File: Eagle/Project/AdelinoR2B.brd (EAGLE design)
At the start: 47 x 53.3 mm, 70 parts, among them J1 DC-044-A, J2 YELLOW-8P-2.54, J3 YELLOW-6P-2.54, J4 YELLOW-8P-2.54, J5 YELLOW-8P-2.54, J6 4P-2.0, J7 YELLOW-2X3P-2.54, J8 4P-2.0, Q1 NCE3407A, Q2 CJ2305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

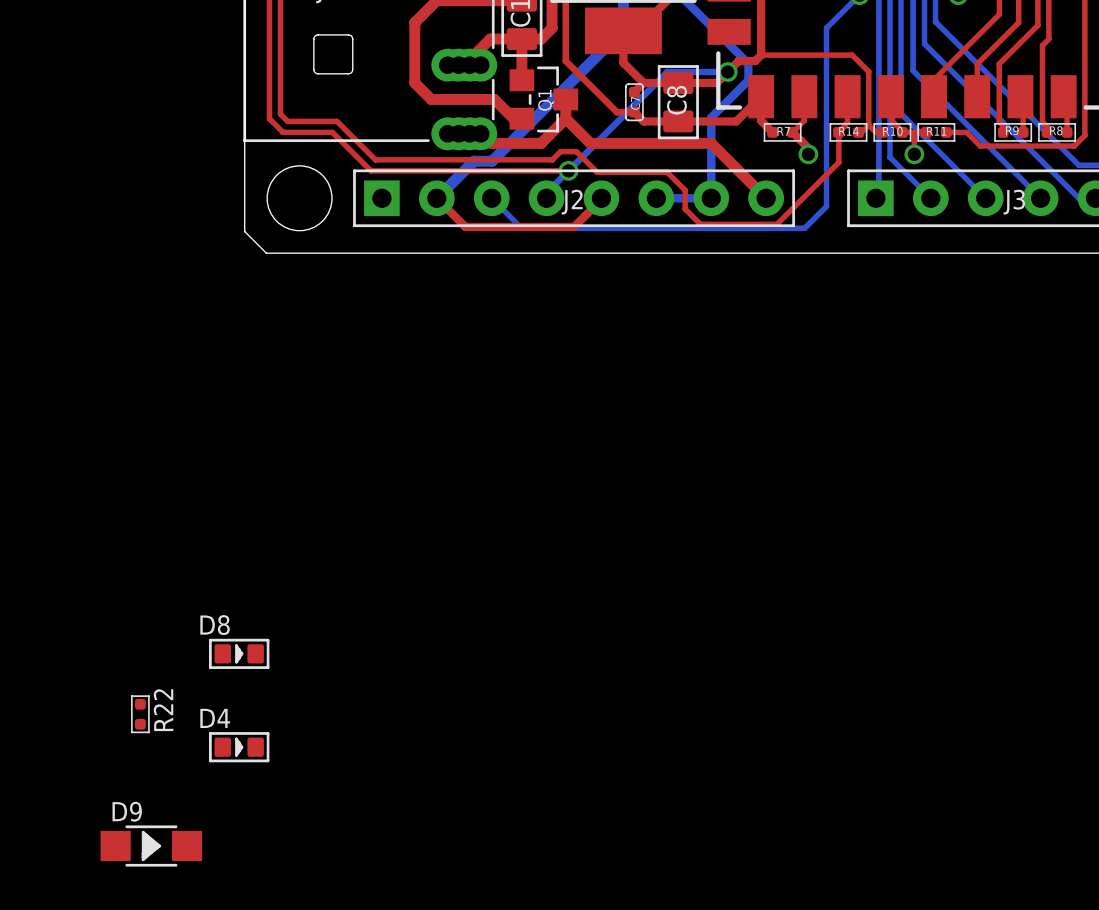
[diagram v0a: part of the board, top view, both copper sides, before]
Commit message: Update GPIO0 wires.
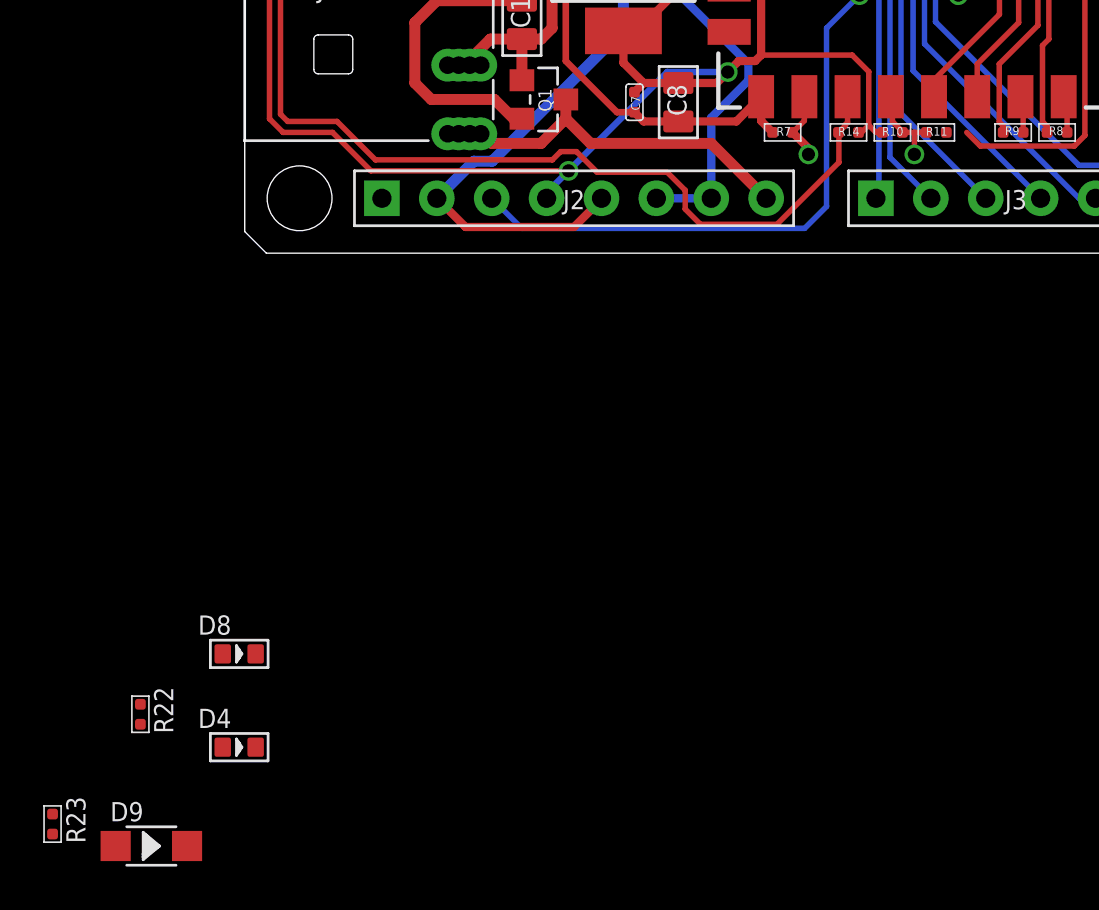
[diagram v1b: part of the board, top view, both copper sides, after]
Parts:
- added R23: 1K, Seeed-Resistor:R0402
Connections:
- new net ESP_PROG: R11.2, R23.2
- net MOSI: no longer R11.2
- net PB0_RX_LED: now also R23.1
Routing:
- net MOSI: track 48.5 -> 47.5 mm
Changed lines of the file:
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@@
 <attribute name="VALUE" x="-6.223" y="-29.464" size="0.889" layer="27" font="vector" ratio="11"/>
+</element>
+<element name="R23" library="Seeed-Resistor" package="R0402" value="1K" x="-8.89" y="-26.416" smashed="yes">
+<attribute name="MPN" value="RC0402JR-071KL" x="-8.89" y="-26.416" size="1.778" layer="27" display="off"/>
+<attribute name="NAME" x="-8.255" y="-25.146" size="0.889" layer="25" ratio="11" rot="R270"/>
+<attribute name="VALUE" x="-10.414" y="-25.146" size="0.889" layer="27" font="vector" ratio="11" rot="R270"/>
 </element>
 </elements>
@@
 <contactref element="U4" pad="10"/>
 <contactref element="J7" pad="5"/>
-<contactref element="R11" pad="2"/>
 <wire x1="44.45" y1="27.94" x2="43.7515" y2="27.2415" width="0.254" layer="1"/>
 <wire x1="43.7515" y1="27.2415" x2="43.033075" y2="27.2415" width="0.254" layer="1"/>
@@
 <wire x1="38.38909375" y1="4.957" x2="34.0411875" y2="4.957" width="0.254" layer="1"/>
 <wire x1="34.0411875" y1="4.957" x2="33.4101875" y2="5.588" width="0.254" layer="1"/>
-<wire x1="33.4101875" y1="5.588" x2="32.4665" y2="5.588" width="0.254" layer="1"/>
 <wire x1="41.41025" y1="26.6065" x2="40.20375" y2="25.4" width="0.254" layer="1"/>
 <wire x1="40.20375" y1="25.4" x2="39.37" y2="25.4" width="0.254" layer="1"/>
@@
 <contactref element="U4" pad="8"/>
 <contactref element="R18" pad="1"/>
+<contactref element="R23" pad="1"/>
 <wire x1="1.9505" y1="27.178" x2="38.312" y2="36.398" width="0" layer="19" extent="1-1"/>
+<wire x1="-8.89" y1="-25.9535" x2="1.9505" y2="27.178" width="0" layer="19" extent="1-1"/>
 </signal>
 <signal name="PD5_TX_LED">
@@
 <wire x1="-4.826" y1="-20.8735" x2="28.512" y2="40.598" width="0" layer="19" extent="1-1"/>
 </signal>
+<signal name="ESP_PROG">
+<contactref element="R23" pad="2"/>
+<contactref element="R11" pad="2"/>
+<wire x1="-8.89" y1="-26.8785" x2="32.4665" y2="5.588" width="0" layer="19" extent="1-1"/>
+</signal>
 </signals>

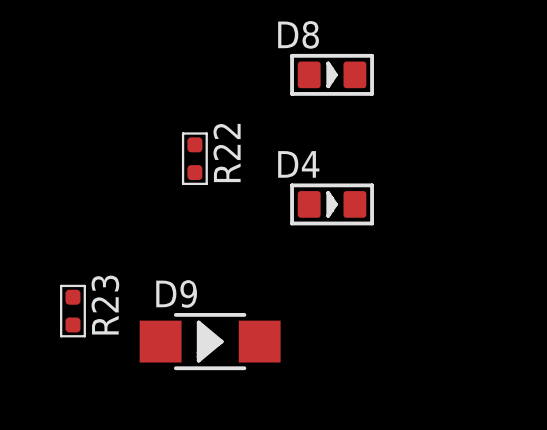
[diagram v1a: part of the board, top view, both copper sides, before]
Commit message: Remove redundant resistor from GPIO0 wiring.
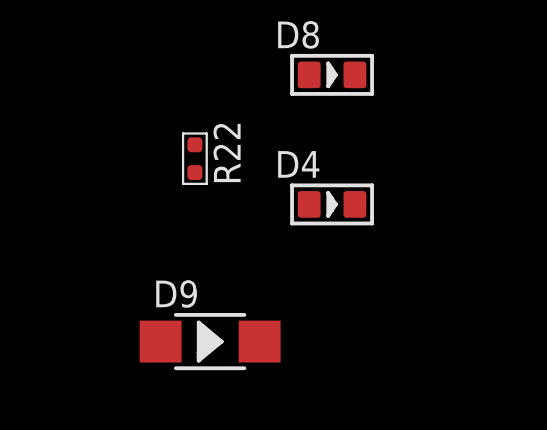
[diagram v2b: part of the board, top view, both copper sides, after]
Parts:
- removed R23: 1K, Seeed-Resistor:R0402
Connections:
- removed net N$6: D5.+, R18.2
- net ESP_PROG: now also D5.+, R18.2; no longer R23.2
- net PB0_RX_LED: no longer R23.1
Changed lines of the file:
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@@
 <attribute name="VALUE" x="-6.223" y="-29.464" size="0.889" layer="27" font="vector" ratio="11"/>
-</element>
-<element name="R23" library="Seeed-Resistor" package="R0402" value="1K" x="-8.89" y="-26.416" smashed="yes">
-<attribute name="MPN" value="RC0402JR-071KL" x="-8.89" y="-26.416" size="1.778" layer="27" display="off"/>
-<attribute name="NAME" x="-8.255" y="-25.146" size="0.889" layer="25" ratio="11" rot="R270"/>
-<attribute name="VALUE" x="-10.414" y="-25.146" size="0.889" layer="27" font="vector" ratio="11" rot="R270"/>
 </element>
 </elements>
@@
 <wire x1="1.9505" y1="29.718" x2="1.524" y2="30.988" width="0" layer="19" extent="1-1"/>
 </signal>
-<signal name="N$6">
-<contactref element="R18" pad="2"/>
-<contactref element="D5" pad="+"/>
-<wire x1="1.524" y1="28.448" x2="2.8755" y2="27.178" width="0" layer="19" extent="1-1"/>
-</signal>
 <signal name="N$8">
 <contactref element="R22" pad="2"/>
@@
 <contactref element="U4" pad="8"/>
 <contactref element="R18" pad="1"/>
-<contactref element="R23" pad="1"/>
 <wire x1="1.9505" y1="27.178" x2="38.312" y2="36.398" width="0" layer="19" extent="1-1"/>
-<wire x1="-8.89" y1="-25.9535" x2="1.9505" y2="27.178" width="0" layer="19" extent="1-1"/>
 </signal>
 <signal name="PD5_TX_LED">
@@
 </signal>
 <signal name="ESP_PROG">
-<contactref element="R23" pad="2"/>
 <contactref element="R11" pad="2"/>
-<wire x1="-8.89" y1="-26.8785" x2="32.4665" y2="5.588" width="0" layer="19" extent="1-1"/>
+<contactref element="R18" pad="2"/>
+<contactref element="D5" pad="+"/>
+<wire x1="2.8755" y1="27.178" x2="32.4665" y2="5.588" width="0" layer="19" extent="1-1"/>
+<wire x1="1.524" y1="28.448" x2="2.8755" y2="27.178" width="0" layer="19" extent="1-1"/>
 </signal>
 </signals>

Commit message: Adding native SPI support.
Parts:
- removed Q3, Q4: MMBT3904LT1G, Seeed-Transistor:SOT-23
- removed R12, R13: 1K, Seeed-Resistor:R0402
- added R23, R24, R25, R26: 1K, Seeed-Resistor:R0402
- R5, R6: value 10K 1/16W -> 10K
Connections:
- removed net HSPI_CLK: U3.5
- removed net HSPI_MISO: U3.6
- removed net HSPI_MOSI: U3.7
- removed net MISO: J7.1, U4.11
- removed net MOSI: J7.5, U4.10
- removed net N$16: Q3.1, R12.2
- removed net N$21: Q4.1, R13.2
- removed net N$4: R7.2, U3.16
- removed net PB0_RX_LED: R18.1, U4.8
- removed net SCK: J7.2, U4.9
- removed net STANDBY1: Q3.3
- removed net STANDBY2: Q4.3
- new net N$15: D5.+, R18.2
- new net N$19: R24.2, U3.7
- new net N$20: R25.2, U3.5
- new net N$22: R26.2, R7.2, U3.16
- new net N$6: R23.2, U3.6
- new net PB0_SS_RX: R18.1, R26.1, U4.8
- new net PB1_SCLK: J7.2, R25.1, U4.9
- new net PB2_MOSI: J7.5, R24.1, U4.10
- new net PB3_MISO: J7.1, R23.1, U4.11
- net ESP_PROG: no longer D5.+, R18.2
- net GND: no longer Q3.2, Q4.2
- net PIN_D13: no longer R13.1
- net PIN_D5: no longer R12.1
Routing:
- net PB2_MOSI: track 0.00 -> 47.5 mm, vias 0 -> 1
- net MOSI: track 47.5 -> 0.00 mm, vias 1 -> 0
- net SCK: track 18.0 -> 0.00 mm, vias 1 -> 0
- net PB1_SCLK: track 0.00 -> 18.0 mm, vias 0 -> 1
- net PB3_MISO: track 0.00 -> 15.1 mm, vias 0 -> 1
- net MISO: track 15.1 -> 0.00 mm, vias 1 -> 0
- net GND: track 296.2 -> 287.0 mm
- net N$20: track 0.00 -> 8.44 mm, vias 0 -> 1
- net HSPI_CLK: track 8.44 -> 0.00 mm, vias 1 -> 0
- net N$6: track 0.00 -> 5.84 mm, vias 0 -> 1
- net HSPI_MISO: track 5.84 -> 0.00 mm, vias 1 -> 0
- net N$19: track 0.00 -> 3.23 mm, vias 0 -> 1
- net HSPI_MOSI: track 3.23 -> 0.00 mm, vias 1 -> 0
- net N$4: track 3.20 -> 0.00 mm, vias 1 -> 0
- net PIN_D5: track 29.3 -> 26.3 mm
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
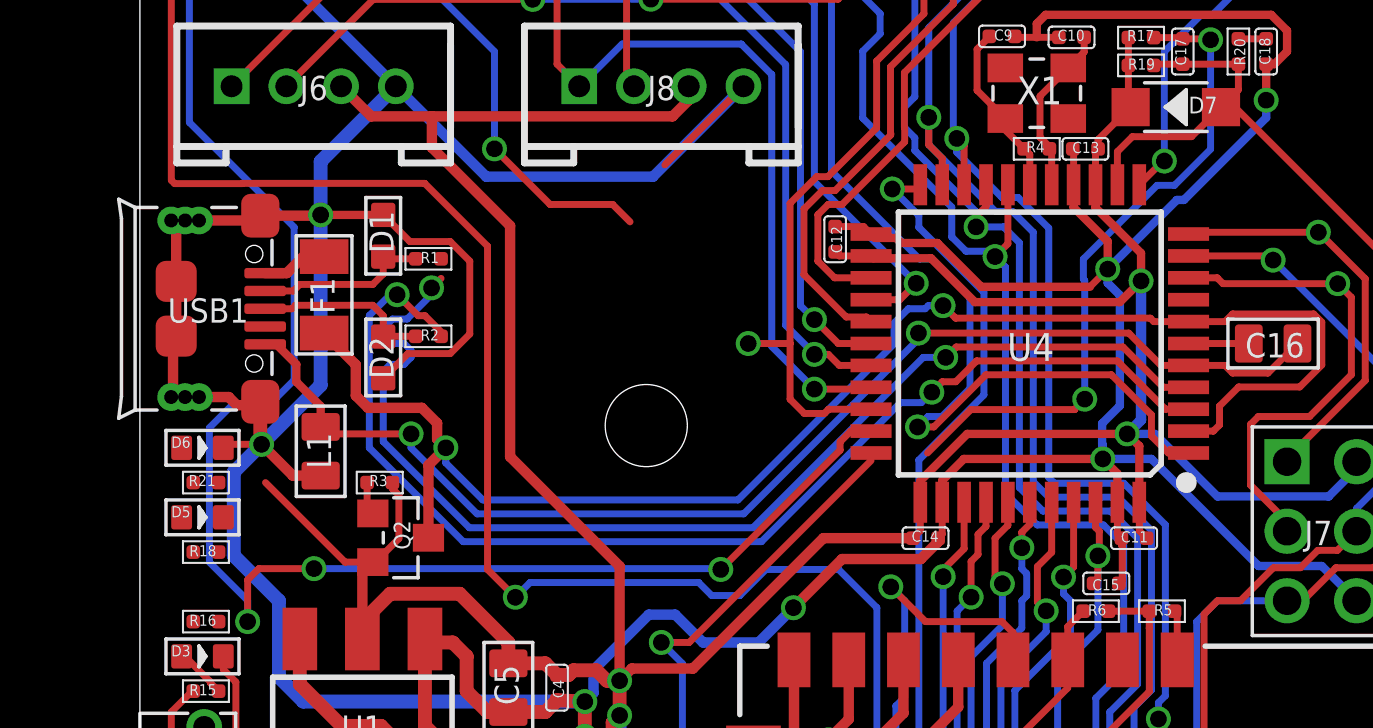
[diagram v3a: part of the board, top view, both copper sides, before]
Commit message: ATmega/Esp control pins reviewed.
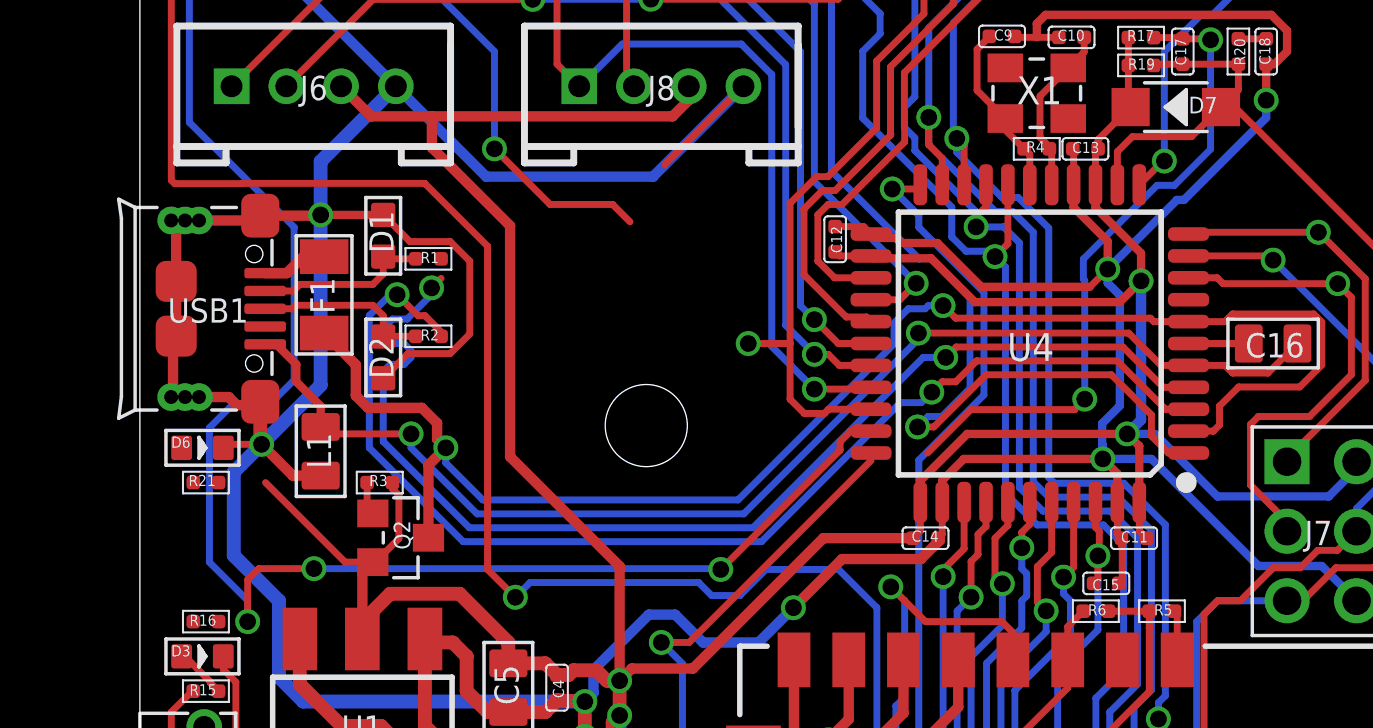
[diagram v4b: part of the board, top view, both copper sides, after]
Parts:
- removed D5: YEL-0603, Seeed-LED:LED-0603
- removed R18: 1K, Seeed-Resistor:R0402
- R14: value 10K 1/16W -> 10K
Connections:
- net PD5_TX_LED renamed ACT_LED
- removed net ESP_PROG: R11.2
- removed net N$15: D5.+, R18.2
- removed net PB0_SS_RX: R18.1, R26.1, U4.8
- new net PB0_SS: R26.1, U4.8
- net +5V: now also R16.1
- net GND: no longer D4.-, D5.-
- net PIN_D13: now also D4.-, R11.2; no longer R16.1
